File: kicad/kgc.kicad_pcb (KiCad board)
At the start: 2 copper layers, 200 x 100 mm, 36 parts, among them IC1 Pico, IC2 MAX7219, IC3 MAX7219

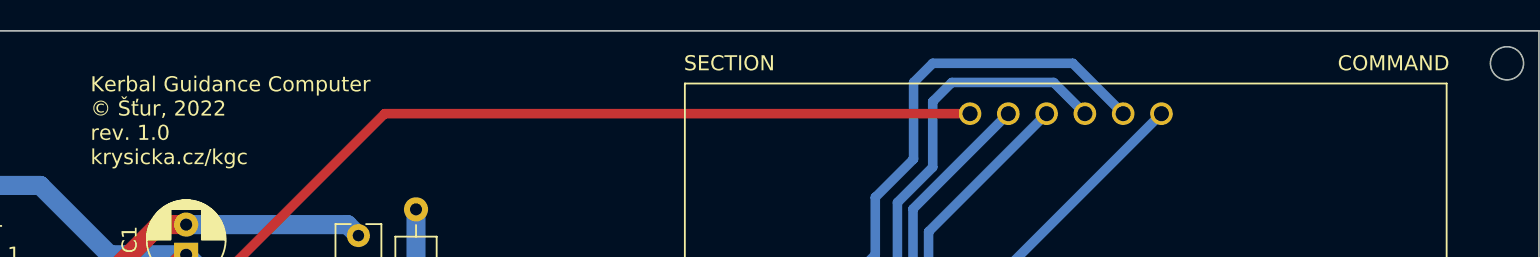
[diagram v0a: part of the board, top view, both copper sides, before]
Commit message: New program switching system, support for LED indicators and buzzer, clear_display now clears individual displays, electrical schematic improvements
kgc.c:
  - New macros for LEDs and buzzer GPIO pins.
  - New function led_init for initializing LEDs and buzzer GPIOs.
  - Section and command system was replaced by verb and nouns (yes, I robed it from AGC). Verbs are commands, nouns are relatively independent parameters for verbs (mostly kind of displayed data) . Verbs are executed by core 0 in main, nouns by core1 in core1_entry.
  - Verbs list:
    - 00 for no operation
    - 01 for display data only
    - 99 for device test
  - Nouns list:
    - 00 for no operation
    - 01 for stopwatch
    - 02 for countdown (doesn't work)

keypad.(h/c):
  - Deleted program and prev_program variables.
  - Renamed section and command variables to verb and noun.

max7219.(h/c):
  - Function clear_display now clears individual display, not whole chip.

kicad:
  - Schematic cleanup.
  - PDF version of schematic included.
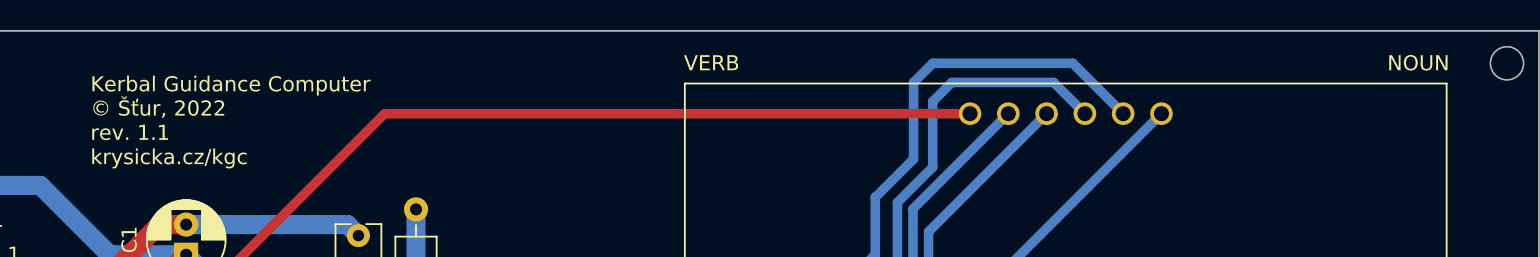
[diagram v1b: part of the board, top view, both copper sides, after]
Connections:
- net /RXD renamed RXD
- net /TXD renamed TXD
- net Net-(BZ1-Pad1) renamed BUZZ
- net Net-(BZ1-Pad2) renamed GND2
- net Net-(C1-Pad2) renamed GND3
- net Net-(DISP1-Pad1) renamed IC2_SEG_E
- net Net-(DISP1-Pad10) renamed IC2_SEG_F
- net Net-(DISP1-Pad11) renamed IC2_SEG_A
- net Net-(DISP1-Pad12) renamed IC2_DIG_0
- net Net-(DISP1-Pad2) renamed IC2_SEG_D
- net Net-(DISP1-Pad3) renamed IC2_SEG_DP
- net Net-(DISP1-Pad4) renamed IC2_SEG_C
- net Net-(DISP1-Pad5) renamed IC2_SEG_G
- net Net-(DISP1-Pad6) renamed IC2_DIG_3
- net Net-(DISP1-Pad7) renamed IC2_SEG_B
- net Net-(DISP1-Pad8) renamed IC2_DIG_2
- net Net-(DISP1-Pad9) renamed IC2_DIG_1
- net Net-(DISP2-Pad12) renamed IC2_DIG_4
- net Net-(DISP2-Pad6) renamed IC2_DIG_7
- net Net-(DISP2-Pad8) renamed IC2_DIG_6
- net Net-(DISP2-Pad9) renamed IC2_DIG_5
- net Net-(DISP3-Pad1) renamed IC3_SEG_E
- net Net-(DISP3-Pad10) renamed IC3_SEG_F
- net Net-(DISP3-Pad11) renamed IC3_SEG_A
- net Net-(DISP3-Pad12) renamed IC3_DIG_0
- net Net-(DISP3-Pad2) renamed IC3_SEG_D
- net Net-(DISP3-Pad3) renamed IC3_SEG_DP
- net Net-(DISP3-Pad4) renamed IC3_SEG_C
- net Net-(DISP3-Pad5) renamed IC3_SEG_G
- net Net-(DISP3-Pad6) renamed IC3_DIG_3
- net Net-(DISP3-Pad7) renamed IC3_SEG_B
- net Net-(DISP3-Pad8) renamed IC3_DIG_2
- net Net-(DISP3-Pad9) renamed IC3_DIG_1
- net Net-(DISP4-Pad12) renamed IC3_DIG_4
- net Net-(DISP4-Pad6) renamed IC3_DIG_7
- net Net-(DISP4-Pad8) renamed IC3_DIG_6
- net Net-(DISP4-Pad9) renamed IC3_DIG_5
- net Net-(IC1-Pad10) renamed LED_ELC
- net Net-(IC1-Pad11) renamed LED_LFO
- net Net-(IC1-Pad12) renamed LED_MOP
- net Net-(IC1-Pad14) renamed LED_OTR
- net Net-(IC1-Pad15) renamed LED_RCS
- net Net-(IC1-Pad16) renamed LED_BRK
- net Net-(IC1-Pad20) renamed KBD_R4
- net Net-(IC1-Pad21) renamed KBD_R3
- net Net-(IC1-Pad22) renamed LOAD_1
- net Net-(IC1-Pad24) renamed CLK
- net Net-(IC1-Pad25) renamed DIN
- net Net-(IC1-Pad26) renamed KBD_R2
- net Net-(IC1-Pad27) renamed KBD_R1
- net Net-(IC1-Pad29) renamed KBD_C4
- net Net-(IC1-Pad3) renamed GND1
- net Net-(IC1-Pad31) renamed KBD_C3
- net Net-(IC1-Pad32) renamed KBD_C2
- net Net-(IC1-Pad34) renamed KBD_C1
- net Net-(IC1-Pad4) renamed LED_CON
- net Net-(IC1-Pad5) renamed LED_FLD
- net Net-(IC1-Pad6) renamed LED_GEA
- net Net-(IC1-Pad7) renamed LOAD_2
- net Net-(IC1-Pad9) renamed LED_SAS
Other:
- board text added: "Kerbal Guidance Computer © Šťur, 2022 rev. 1.1 krysicka.cz/kgc"
- board text added: "NOUN"
- board text added: "VERB"
- board text removed: "COMMAND"
- board text removed: "Kerbal Guidance Computer © Šťur, 2022 rev. 1.0 krysicka.cz/kgc"
- board text removed: "SECTION"

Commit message: Added KiCad project files
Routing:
- net IC2_DIG_4: track 52.5 -> 53.6 mm

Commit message: New hardware revision
- Created new PCB
- KiCad project updated
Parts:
- removed IC1: Pico, mistniBordel:RPi_Pico_TH
- removed IC2, IC3: MAX7219, Package_DIP:DIP-24_W7.62mm
- removed KBD1: ak1604, Connector_PinHeader_2.54mm:PinHeader_1x08_P2.54mm_Vertical
- removed UART1: UART, Connector_PinHeader_2.54mm:PinHeader_1x04_P2.54mm_Horizontal
- added C10: 100n, Capacitor_SMD:C_0603_1608Metric_Pad1.08x0.95mm_HandSolder, B.Cu at (198.1, 86.7)
- added C11: 100n, Capacitor_SMD:C_0603_1608Metric_Pad1.08x0.95mm_HandSolder, B.Cu at (191.2, 99.9)
- added C12: 100n, Capacitor_SMD:C_0603_1608Metric_Pad1.08x0.95mm_HandSolder, B.Cu at (197.5, 91.4)
- added C13: 100n, Capacitor_SMD:C_0603_1608Metric_Pad1.08x0.95mm_HandSolder, B.Cu at (179.5, 93.4)
- added C14: 100n, Capacitor_SMD:C_0603_1608Metric_Pad1.08x0.95mm_HandSolder, B.Cu at (188.4, 98.5)
- added C15: 4.7u, Capacitor_SMD:C_0603_1608Metric_Pad1.08x0.95mm_HandSolder, B.Cu at (182.3, 81.1)
- added C16: 4.7u, Capacitor_SMD:C_0603_1608Metric_Pad1.08x0.95mm_HandSolder, B.Cu at (175.5, 81.1)
- added C17: 4.7u, Capacitor_SMD:C_0603_1608Metric_Pad1.08x0.95mm_HandSolder, B.Cu at (179.5, 87.9)
- added C18: 15p, Capacitor_SMD:C_0603_1608Metric_Pad1.08x0.95mm_HandSolder, B.Cu at (192.0, 105.9)
- added C19: 15p, Capacitor_SMD:C_0603_1608Metric_Pad1.08x0.95mm_HandSolder, B.Cu at (185.6, 105.9)
- added C20: 100n, Capacitor_SMD:C_0603_1608Metric_Pad1.08x0.95mm_HandSolder, B.Cu at (197.2, 73.9)
- added C21: 100 nF, Capacitor_SMD:C_0603_1608Metric_Pad1.08x0.95mm_HandSolder, B.Cu at (160.2, 45.4)
- added C22: 4.7 uF, Capacitor_SMD:CP_Elec_5x4.5, B.Cu at (158.2, 51.3)
- added C23: 100 nF, Capacitor_SMD:C_0603_1608Metric_Pad1.08x0.95mm_HandSolder, B.Cu at (162.3, 44.4)
- added C24: 10 uF, Capacitor_SMD:CP_Elec_5x4.5, B.Cu at (276.1, 52.5)
- added C25: 0.1 uF, Capacitor_SMD:C_0603_1608Metric_Pad1.08x0.95mm_HandSolder, B.Cu at (268.2, 63.4)
- added C26: 10 uF, Capacitor_SMD:CP_Elec_5x4.5, B.Cu at (221.9, 108.9)
- added C27: 0.1 uF, Capacitor_SMD:C_0603_1608Metric_Pad1.08x0.95mm_HandSolder, B.Cu at (214.1, 119.9)
- added C28: 10 uF, Capacitor_SMD:CP_Elec_5x4.5, B.Cu at (221.9, 70.6)
- added C29: 0.1 uF, Capacitor_SMD:C_0603_1608Metric_Pad1.08x0.95mm_HandSolder, B.Cu at (214.1, 81.2)
- added C5: 100n, Capacitor_SMD:C_0603_1608Metric_Pad1.08x0.95mm_HandSolder, B.Cu at (185.6, 99.6)
- added C6: 100n, Capacitor_SMD:C_0603_1608Metric_Pad1.08x0.95mm_HandSolder, B.Cu at (179.5, 84.0)
- added C7: 100n, Capacitor_SMD:C_0603_1608Metric_Pad1.08x0.95mm_HandSolder, B.Cu at (179.5, 86.1)
- added C8: 100n, Capacitor_SMD:C_0603_1608Metric_Pad1.08x0.95mm_HandSolder, B.Cu at (179.5, 89.8)
- added C9: 100n, Capacitor_SMD:C_0603_1608Metric_Pad1.08x0.95mm_HandSolder, B.Cu at (191.4, 81.1)
- added D11: 1N5819, Diode_THT:D_DO-41_SOD81_P7.62mm_Horizontal, B.Cu at (313.2, 191.3)
- added D12: 1N5819, Diode_THT:D_DO-41_SOD81_P7.62mm_Horizontal, B.Cu at (188.2, 178.8)
- added D13: 1N5819, Diode_THT:D_DO-41_SOD81_P7.62mm_Horizontal, B.Cu at (213.3, 178.8)
- added D14: 1N5819, Diode_THT:D_DO-41_SOD81_P7.62mm_Horizontal, B.Cu at (238.3, 178.8)
- added D15: 1N5819, Diode_THT:D_DO-41_SOD81_P7.62mm_Horizontal, B.Cu at (263.3, 178.8)
- added D16: 1N5819, Diode_THT:D_DO-41_SOD81_P7.62mm_Horizontal, B.Cu at (288.3, 178.8)
- added D17: 1N5819, Diode_THT:D_DO-41_SOD81_P7.62mm_Horizontal, B.Cu at (188.2, 203.7)
- added D18: 1N5819, Diode_THT:D_DO-41_SOD81_P7.62mm_Horizontal, B.Cu at (213.2, 203.8)
- added D19: 1N5819, Diode_THT:D_DO-41_SOD81_P7.62mm_Horizontal, B.Cu at (238.3, 203.7)
- added D20: 1N5819, Diode_THT:D_DO-41_SOD81_P7.62mm_Horizontal, B.Cu at (263.4, 203.7)
- added D21: 1N5819, Diode_THT:D_DO-41_SOD81_P7.62mm_Horizontal, B.Cu at (288.3, 203.7)
- added D22: CON, LED_SMD:LED_0805_2012Metric_Pad1.15x1.40mm_HandSolder, F.Cu at (164.6, 50.6)
- added D23: FLD, LED_SMD:LED_0805_2012Metric_Pad1.15x1.40mm_HandSolder, F.Cu at (203.1, 50.6)
- added D24: ELC, LED_SMD:LED_0805_2012Metric_Pad1.15x1.40mm_HandSolder, F.Cu at (164.6, 70.5)
- added D25: MOP, LED_SMD:LED_0805_2012Metric_Pad1.15x1.40mm_HandSolder, F.Cu at (203.1, 70.5)
- added D26: LFO, LED_SMD:LED_0805_2012Metric_Pad1.15x1.40mm_HandSolder, F.Cu at (164.6, 90.3)
- added D27: OTR, LED_SMD:LED_0805_2012Metric_Pad1.15x1.40mm_HandSolder, F.Cu at (203.1, 90.3)
- added D28: SAS, LED_SMD:LED_0805_2012Metric_Pad1.15x1.40mm_HandSolder, F.Cu at (164.6, 110.2)
- added D29: RCS, LED_SMD:LED_0805_2012Metric_Pad1.15x1.40mm_HandSolder, F.Cu at (203.1, 110.2)
- added D30: GEA, LED_SMD:LED_0805_2012Metric_Pad1.15x1.40mm_HandSolder, F.Cu at (164.6, 130.0)
- added D31: BRK, LED_SMD:LED_0805_2012Metric_Pad1.15x1.40mm_HandSolder, F.Cu at (203.1, 130.0)
- added DISP10: OPD-D5631YG-BW, Display_7Segment:DA56-11CGKWA, F.Cu at (240.3, 138.1)
- added DISP11: OPD-D5631YG-BW, Display_7Segment:DA56-11CGKWA, F.Cu at (266.1, 138.1)
- added DISP12: OPD-D5631YG-BW, Display_7Segment:DA56-11CGKWA, F.Cu at (291.9, 138.1)
- added DISP5: OPD-D5631YG-BW, Display_7Segment:DA56-11CGKWA, F.Cu at (266.1, 98.1)
- added DISP6: OPD-D5631YG-BW, Display_7Segment:DA56-11CGKWA, F.Cu at (291.9, 98.1)
- added DISP7: OPD-D5631YG-BW, Display_7Segment:DA56-11CGKWA, F.Cu at (240.3, 118.1)
- added DISP8: OPD-D5631YG-BW, Display_7Segment:DA56-11CGKWA, F.Cu at (266.1, 118.1)
- added DISP9: OPD-D5631YG-BW, Display_7Segment:DA56-11CGKWA, F.Cu at (291.9, 118.1)
- added H1: MountingHole, MountingHole:MountingHole_3.2mm_M3, F.Cu at (135.0, 35.0)
- added H2: MountingHole, MountingHole:MountingHole_3.2mm_M3, F.Cu at (325.0, 35.0)
- added H3: MountingHole, MountingHole:MountingHole_3.2mm_M3, F.Cu at (325.0, 235.0)
- added H4: MountingHole, MountingHole:MountingHole_3.2mm_M3, F.Cu at (135.0, 235.0)
- added J1: Conn_01x04_Pin, Connector_PinHeader_2.54mm:PinHeader_1x04_P2.54mm_Horizontal, B.Cu at (159.3, 89.0)
- added J2: SM03B-SRSS-TB, Connector_JST:JST_SH_SM03B-SRSS-TB_1x03-1MP_P1.00mm_Horizontal, B.Cu at (157.2, 103.2)
- added J4: USB_C_Receptacle_USB2.0_16P, Connector_USB:USB_C_Receptacle_GCT_USB4085, B.Cu at (175.0, 36.1)
- added J5: USB_C_Receptacle_USB2.0_16P, Connector_USB:USB_C_Receptacle_GCT_USB4085, B.Cu at (150.0, 36.1)
- added L1: 3.3u, RP2350_80QFN:L_pol_2016, B.Cu at (179.3, 81.2)
- added R13: 5k, Resistor_SMD:R_0603_1608Metric_Pad0.98x0.95mm_HandSolder, F.Cu at (153.0, 32.1)
- added R14: 27R, Resistor_SMD:R_0603_1608Metric_Pad0.98x0.95mm_HandSolder, B.Cu at (157.9, 40.4)
- added R15: 27R, Resistor_SMD:R_0603_1608Metric_Pad0.98x0.95mm_HandSolder, B.Cu at (152.4, 40.4)
- added R16: 270R, Resistor_SMD:R_0603_1608Metric_Pad0.98x0.95mm_HandSolder, B.Cu at (139.8, 43.4)
- added R17: 270R, Resistor_SMD:R_0603_1608Metric_Pad0.98x0.95mm_HandSolder, B.Cu at (139.8, 45.9)
- added R18: 1k, Resistor_SMD:R_0603_1608Metric_Pad0.98x0.95mm_HandSolder, B.Cu at (182.8, 143.7)
- added R19: 1k, Resistor_SMD:R_0603_1608Metric_Pad0.98x0.95mm_HandSolder, B.Cu at (185.4, 143.7)
- added R20: 1k, Resistor_SMD:R_0603_1608Metric_Pad0.98x0.95mm_HandSolder, B.Cu at (187.9, 143.7)
- added R21: 1k, Resistor_SMD:R_0603_1608Metric_Pad0.98x0.95mm_HandSolder, B.Cu at (190.5, 143.7)
- added R22: 1k, Resistor_SMD:R_0603_1608Metric_Pad0.98x0.95mm_HandSolder, B.Cu at (193.0, 143.7)
- added R23: 1k, Resistor_SMD:R_0603_1608Metric_Pad0.98x0.95mm_HandSolder, B.Cu at (195.5, 143.7)
- added R24: 1k, Resistor_SMD:R_0603_1608Metric_Pad0.98x0.95mm_HandSolder, B.Cu at (198.1, 143.7)
- added R25: 10k, Resistor_SMD:R_0603_1608Metric_Pad0.98x0.95mm_HandSolder, B.Cu at (268.2, 65.1)
- added R26: 10k, Resistor_SMD:R_0603_1608Metric_Pad0.98x0.95mm_HandSolder, B.Cu at (214.1, 121.5)
- added R27: 10k, Resistor_SMD:R_0603_1608Metric_Pad0.98x0.95mm_HandSolder, B.Cu at (214.1, 82.8)
- added R28: 100R, Resistor_SMD:R_0603_1608Metric_Pad0.98x0.95mm_HandSolder, F.Cu at (171.6, 50.6)
- added R29: 100R, Resistor_SMD:R_0603_1608Metric_Pad0.98x0.95mm_HandSolder, F.Cu at (210.1, 50.6)
- added R30: 100R, Resistor_SMD:R_0603_1608Metric_Pad0.98x0.95mm_HandSolder, F.Cu at (171.6, 70.5)
- added R31: 100R, Resistor_SMD:R_0603_1608Metric_Pad0.98x0.95mm_HandSolder, F.Cu at (210.1, 70.5)
- added R32: 100R, Resistor_SMD:R_0603_1608Metric_Pad0.98x0.95mm_HandSolder, F.Cu at (171.6, 90.3)
- added R33: 100R, Resistor_SMD:R_0603_1608Metric_Pad0.98x0.95mm_HandSolder, F.Cu at (210.1, 90.3)
- added R34: 100R, Resistor_SMD:R_0603_1608Metric_Pad0.98x0.95mm_HandSolder, F.Cu at (171.6, 110.2)
- added R35: 100R, Resistor_SMD:R_0603_1608Metric_Pad0.98x0.95mm_HandSolder, F.Cu at (210.1, 110.2)
- added R36: 100R, Resistor_SMD:R_0603_1608Metric_Pad0.98x0.95mm_HandSolder, F.Cu at (171.6, 130.0)
- added R37: 100R, Resistor_SMD:R_0603_1608Metric_Pad0.98x0.95mm_HandSolder, F.Cu at (210.1, 130.0)
- added SW1: TS6606, Button_Switch_THT:SW_Tactile_SKHH_Angled, B.Cu at (283.4, 32.8)
- added SW10: ., other_things:SW_Cherry_MX_1.00u_PCB, F.Cu at (182.5, 184.9)
- added SW11: 4, other_things:SW_Cherry_MX_1.00u_PCB, F.Cu at (207.5, 184.9)
- added SW12: 5, other_things:SW_Cherry_MX_1.00u_PCB, F.Cu at (232.5, 184.9)
- added SW13: 6, other_things:SW_Cherry_MX_1.00u_PCB, F.Cu at (257.5, 184.9)
- added SW14: PRO, other_things:SW_Cherry_MX_1.00u_PCB, F.Cu at (282.5, 184.9)
- added SW15: NOUN, other_things:SW_Cherry_MX_1.00u_PCB, F.Cu at (157.5, 197.4)
- added SW16: ALRM, other_things:SW_Cherry_MX_1.00u_PCB, F.Cu at (307.5, 197.4)
- added SW17: 0, other_things:SW_Cherry_MX_1.00u_PCB, F.Cu at (182.5, 209.9)
- added SW18: 1, other_things:SW_Cherry_MX_1.00u_PCB, F.Cu at (207.5, 209.9)
- added SW19: 2, other_things:SW_Cherry_MX_1.00u_PCB, F.Cu at (232.5, 209.9)
- added SW2: TS6606, Button_Switch_THT:SW_Tactile_SKHH_Angled, B.Cu at (308.4, 32.8)
- added SW20: 3, other_things:SW_Cherry_MX_1.00u_PCB, F.Cu at (257.5, 209.9)
- added SW21: RSET, other_things:SW_Cherry_MX_1.00u_PCB, F.Cu at (282.5, 209.9)
- added SW3: -, other_things:SW_Cherry_MX_1.00u_PCB, F.Cu at (182.5, 159.9)
- added SW4: 7, other_things:SW_Cherry_MX_1.00u_PCB, F.Cu at (207.5, 159.9)
- added SW5: 8, other_things:SW_Cherry_MX_1.00u_PCB, F.Cu at (232.5, 159.9)
- added SW6: 9, other_things:SW_Cherry_MX_1.00u_PCB, F.Cu at (257.5, 159.9)
- added SW7: CLR, other_things:SW_Cherry_MX_1.00u_PCB, F.Cu at (282.5, 159.9)
- added SW8: VERB, other_things:SW_Cherry_MX_1.00u_PCB, F.Cu at (157.5, 172.4)
- added SW9: ENTR, other_things:SW_Cherry_MX_1.00u_PCB, F.Cu at (307.5, 172.4)
- added TP1: TestPoint, TestPoint:TestPoint_Plated_Hole_D2.0mm, F.Cu at (279.5, 75.7)
- added TP2: TestPoint, TestPoint:TestPoint_Plated_Hole_D2.0mm, F.Cu at (149.2, 48.0)
- added TP3: TestPoint, TestPoint:TestPoint_Plated_Hole_D2.0mm, F.Cu at (214.1, 135.2)
- added TP4: TestPoint, TestPoint:TestPoint_Plated_Hole_D2.0mm, F.Cu at (160.7, 59.5)
- added TP5: TestPoint, TestPoint:TestPoint_Plated_Hole_D2.0mm, F.Cu at (225.6, 99.0)
- added TP6: TestPoint, TestPoint:TestPoint_Plated_Hole_D2.0mm, F.Cu at (181.2, 60.7)
- added TP7: TestPoint, TestPoint:TestPoint_Plated_Hole_D2.0mm, F.Cu at (208.4, 99.0)
- added TP8: TestPoint, TestPoint:TestPoint_Plated_Hole_D2.0mm, F.Cu at (148.5, 54.8)
- added TP9: TestPoint, TestPoint:TestPoint_Plated_Hole_D2.0mm, F.Cu at (217.0, 99.0)
- added U1: NCP1117-3.3_SOT223, Package_TO_SOT_SMD:SOT-223-3_TabPin2, B.Cu at (166.3, 63.2)
- added U2: RP2350_80QFN, RP2350_80QFN:RP2350-QFN-80-1EP_10x10_P0.4mm_EP3.4x3.4mm_ThermalVias, B.Cu at (188.5, 89.6)
- added U3: W25Q128JVS, Package_SO:SOIC-8_5.3x5.3mm_P1.27mm, B.Cu at (201.9, 77.9)
- added U4: FT230XS, Package_SO:SSOP-16_3.9x4.9mm_P0.635mm, B.Cu at (155.1, 44.9)
- added U5: MAX7221xWG, Package_SO:SOIC-24W_7.5x15.4mm_P1.27mm, B.Cu at (276.3, 64.0)
- added U6: MAX7221xWG, Package_SO:SOIC-24W_7.5x15.4mm_P1.27mm, B.Cu at (222.1, 120.5)
- added U7: MAX7221xWG, Package_SO:SOIC-24W_7.5x15.4mm_P1.27mm, B.Cu at (222.2, 81.8)
- added Y1: ABM8-272-T3, Crystal:Crystal_SMD_3225-4Pin_3.2x2.5mm, B.Cu at (188.8, 106.1)
- BZ1: footprint Buzzer_Beeper:Buzzer_12x9.5RM7.6 -> other_things:Buzzer_XDCR_CPT-1203-03-SMT-TR; moved to B.Cu
- C1: value 10 uF -> 10u; footprint Capacitor_THT:CP_Radial_D5.0mm_P2.00mm -> Capacitor_SMD:C_0603_1608Metric_Pad1.08x0.95mm_HandSolder; moved to B.Cu
- C2: value 0.1 uF -> 10u; footprint mistniBordel:C31x -> Capacitor_SMD:C_0603_1608Metric_Pad1.08x0.95mm_HandSolder; moved to B.Cu
- C3: value 10 uF -> 100n; footprint Capacitor_THT:CP_Radial_D5.0mm_P2.00mm -> Capacitor_SMD:C_0603_1608Metric_Pad1.08x0.95mm_HandSolder; moved to B.Cu
- C4: value 0.1 uF -> 4.7u; footprint mistniBordel:C31x -> Capacitor_SMD:C_0603_1608Metric_Pad1.08x0.95mm_HandSolder; moved to B.Cu
- D1: value CON -> RXLED; footprint LED_THT:LED_D5.0mm -> LED_SMD:LED_0603_1608Metric; moved to B.Cu
- D10: value BRK -> 1N5819; footprint LED_THT:LED_D5.0mm -> Diode_THT:D_DO-41_SOD81_P7.62mm_Horizontal; moved to B.Cu
- D2: value FLD -> TXLED; footprint LED_THT:LED_D5.0mm -> LED_SMD:LED_0603_1608Metric; moved to B.Cu
- D3: value ELC -> 1N5819; footprint LED_THT:LED_D5.0mm -> Diode_THT:D_DO-41_SOD81_P7.62mm_Horizontal; moved to B.Cu
- D4: value MOP -> 1N5819; footprint LED_THT:LED_D5.0mm -> Diode_THT:D_DO-41_SOD81_P7.62mm_Horizontal; moved to B.Cu
- D5: value LFO -> 1N5819; footprint LED_THT:LED_D5.0mm -> Diode_THT:D_DO-41_SOD81_P7.62mm_Horizontal; moved to B.Cu
- D6: value OTR -> 1N5819; footprint LED_THT:LED_D5.0mm -> Diode_THT:D_DO-41_SOD81_P7.62mm_Horizontal; moved to B.Cu
- D7: value SAS -> 1N5819; footprint LED_THT:LED_D5.0mm -> Diode_THT:D_DO-41_SOD81_P7.62mm_Horizontal; moved to B.Cu
- D8: value RCS -> 1N5819; footprint LED_THT:LED_D5.0mm -> Diode_THT:D_DO-41_SOD81_P7.62mm_Horizontal; moved to B.Cu
- D9: value GEA -> 1N5819; footprint LED_THT:LED_D5.0mm -> Diode_THT:D_DO-41_SOD81_P7.62mm_Horizontal; moved to B.Cu
- DISP1, DISP2, DISP3, DISP4: value CC56-12GWA -> OPD-D5631YG-BW; footprint Display_7Segment:CC56-12GWA -> Display_7Segment:DA56-11CGKWA
- R1: value 100R -> 33; footprint Resistor_THT:R_Axial_DIN0207_L6.3mm_D2.5mm_P10.16mm_Horizontal -> Resistor_SMD:R_0603_1608Metric_Pad0.98x0.95mm_HandSolder; moved to B.Cu
- R10: value 100R -> 5k; footprint Resistor_THT:R_Axial_DIN0207_L6.3mm_D2.5mm_P10.16mm_Horizontal -> Resistor_SMD:R_0603_1608Metric_Pad0.98x0.95mm_HandSolder
- R11: value 10k -> 5k; footprint Resistor_THT:R_Axial_DIN0207_L6.3mm_D2.5mm_P10.16mm_Horizontal -> Resistor_SMD:R_0603_1608Metric_Pad0.98x0.95mm_HandSolder
- R12: value 10k -> 5k; footprint Resistor_THT:R_Axial_DIN0207_L6.3mm_D2.5mm_P10.16mm_Horizontal -> Resistor_SMD:R_0603_1608Metric_Pad0.98x0.95mm_HandSolder; moved to B.Cu
- R2, R3: value 100R -> 27R; footprint Resistor_THT:R_Axial_DIN0207_L6.3mm_D2.5mm_P10.16mm_Horizontal -> Resistor_SMD:R_0603_1608Metric_Pad0.98x0.95mm_HandSolder; moved to B.Cu
- R4, R5, R6: value 100R -> 1k; footprint Resistor_THT:R_Axial_DIN0207_L6.3mm_D2.5mm_P10.16mm_Horizontal -> Resistor_SMD:R_0603_1608Metric_Pad0.98x0.95mm_HandSolder; moved to B.Cu
- R7, R8: value 100R -> DNF; footprint Resistor_THT:R_Axial_DIN0207_L6.3mm_D2.5mm_P10.16mm_Horizontal -> Resistor_SMD:R_0603_1608Metric_Pad0.98x0.95mm_HandSolder; moved to B.Cu
- R9: value 100R -> 0R; footprint Resistor_THT:R_Axial_DIN0207_L6.3mm_D2.5mm_P10.16mm_Horizontal -> Resistor_SMD:R_0603_1608Metric_Pad0.98x0.95mm_HandSolder; moved to B.Cu
- moved D4 248.0 mm to (313.2, 166.1), turned to 180 degrees
- moved R5 240.1 mm to (300.4, 32.9)
- moved D9 235.2 mm to (288.3, 153.8), turned to 180 degrees
- moved D7 187.5 mm to (238.3, 153.8), turned to 180 degrees
- moved D8 187.1 mm to (263.3, 153.8), turned to 180 degrees
- moved R4 186.3 mm to (275.4, 32.9)
- moved R9 144.1 mm to (201.9, 81.8), turned to 0 degrees
- moved D5 143.8 mm to (188.3, 153.8), turned to 180 degrees
- moved D6 143.4 mm to (213.3, 153.8), turned to 180 degrees
- moved R7 141.6 mm to (203.2, 72.1), turned to 0 degrees
- moved D3 136.6 mm to (163.3, 166.2), turned to 180 degrees
- moved R10 129.6 mm to (174.3, 38.6)
- moved R8 119.1 mm to (204.9, 73.9)
- moved R3 115.1 mm to (186.1, 81.1), turned to 90 degrees
- moved R1 109.4 mm to (180.0, 76.7), turned to 0 degrees
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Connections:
- BZ1 pad 1: BUZZ -> /BUZZ
- BZ1 pad 2: GND2 -> GND
- C1 pad 1: +5V -> VBUS
- C1 pad 2: GND3 -> GND
- C2 pad 1: +5V -> +3V3
- C2 pad 2: GND3 -> GND
- C3 pad 1: +5V -> +1V1
- C3 pad 2: GND3 -> GND
- C4 pad 1: +5V -> +1V1
- C4 pad 2: GND3 -> GND
- D1 pad 1: GND2 -> Net-(D1-K)
- D1 pad 2: Net-(D1-Pad2) -> Net-(D1-A)
- D10 pad 1: GND2 -> /KBD_ROW_2
- D10 pad 2: Net-(D10-Pad2) -> Net-(D10-A)
- D2 pad 1: GND2 -> Net-(D2-K)
- D2 pad 2: Net-(D2-Pad2) -> Net-(D2-A)
- D3 pad 1: GND2 -> /KBD_ROW_1
- D3 pad 2: Net-(D3-Pad2) -> Net-(D3-A)
- D4 pad 1: GND2 -> /KBD_ROW_1
- D4 pad 2: Net-(D4-Pad2) -> Net-(D4-A)
- D5 pad 1: GND2 -> /KBD_ROW_1
- D5 pad 2: Net-(D5-Pad2) -> Net-(D5-A)
- D6 pad 1: GND2 -> /KBD_ROW_1
- D6 pad 2: Net-(D6-Pad2) -> Net-(D6-A)
- D7 pad 1: GND2 -> /KBD_ROW_1
- D7 pad 2: Net-(D7-Pad2) -> Net-(D7-A)
- D8 pad 1: GND2 -> /KBD_ROW_1
- D8 pad 2: Net-(D8-Pad2) -> Net-(D8-A)
- D9 pad 1: GND2 -> /KBD_ROW_1
- D9 pad 2: Net-(D9-Pad2) -> Net-(D9-A)
- DISP1 pad 1: IC2_SEG_E -> /Displays and LEDs/MAX3_SEG_E
- DISP1 pad 10: IC2_SEG_F -> /Displays and LEDs/MAX3_SEG_B
- DISP1 pad 11: IC2_SEG_A -> /Displays and LEDs/MAX3_SEG_A
- DISP1 pad 12: IC2_DIG_0 -> /Displays and LEDs/MAX3_SEG_F
- DISP1 pad 2: IC2_SEG_D -> /Displays and LEDs/MAX3_SEG_D
- DISP1 pad 3: IC2_SEG_DP -> /Displays and LEDs/MAX3_SEG_C
- DISP1 pad 4: IC2_SEG_C -> /Displays and LEDs/MAX3_SEG_DP
- DISP1 pad 5: IC2_SEG_G -> /Displays and LEDs/MAX3_SEG_E
- DISP1 pad 6: IC2_DIG_3 -> /Displays and LEDs/MAX3_SEG_D
- DISP1 pad 7: IC2_SEG_B -> /Displays and LEDs/MAX3_SEG_G
- DISP1 pad 8: IC2_DIG_2 -> /Displays and LEDs/MAX3_SEG_C
- DISP1 pad 9: IC2_DIG_1 -> /Displays and LEDs/MAX3_SEG_DP
- DISP2 pad 1: IC2_SEG_E -> /Displays and LEDs/MAX1_SEG_E
- DISP2 pad 10: IC2_SEG_F -> /Displays and LEDs/MAX1_SEG_B
- DISP2 pad 11: IC2_SEG_A -> /Displays and LEDs/MAX1_SEG_A
- DISP2 pad 12: IC2_DIG_4 -> /Displays and LEDs/MAX1_SEG_F
- DISP2 pad 2: IC2_SEG_D -> /Displays and LEDs/MAX1_SEG_D
- DISP2 pad 3: IC2_SEG_DP -> /Displays and LEDs/MAX1_SEG_C
- DISP2 pad 4: IC2_SEG_C -> /Displays and LEDs/MAX1_SEG_DP
- DISP2 pad 5: IC2_SEG_G -> /Displays and LEDs/MAX1_SEG_E
- DISP2 pad 6: IC2_DIG_7 -> /Displays and LEDs/MAX1_SEG_D
- DISP2 pad 7: IC2_SEG_B -> /Displays and LEDs/MAX1_SEG_G
- DISP2 pad 8: IC2_DIG_6 -> /Displays and LEDs/MAX1_SEG_C
- DISP2 pad 9: IC2_DIG_5 -> /Displays and LEDs/MAX1_SEG_DP
- DISP3 pad 1: IC3_SEG_E -> /Displays and LEDs/MAX1_SEG_E
- DISP3 pad 10: IC3_SEG_F -> /Displays and LEDs/MAX1_SEG_B
- DISP3 pad 11: IC3_SEG_A -> /Displays and LEDs/MAX1_SEG_A
- DISP3 pad 12: IC3_DIG_0 -> /Displays and LEDs/MAX1_SEG_F
- DISP3 pad 2: IC3_SEG_D -> /Displays and LEDs/MAX1_SEG_D
- DISP3 pad 3: IC3_SEG_DP -> /Displays and LEDs/MAX1_SEG_C
- DISP3 pad 4: IC3_SEG_C -> /Displays and LEDs/MAX1_SEG_DP
- DISP3 pad 5: IC3_SEG_G -> /Displays and LEDs/MAX1_SEG_E
- DISP3 pad 6: IC3_DIG_3 -> /Displays and LEDs/MAX1_SEG_D
- DISP3 pad 7: IC3_SEG_B -> /Displays and LEDs/MAX1_SEG_G
- DISP3 pad 8: IC3_DIG_2 -> /Displays and LEDs/MAX1_SEG_C
- DISP3 pad 9: IC3_DIG_1 -> /Displays and LEDs/MAX1_SEG_DP
- DISP4 pad 1: IC3_SEG_E -> /Displays and LEDs/MAX3_SEG_E
- DISP4 pad 10: IC3_SEG_F -> /Displays and LEDs/MAX3_SEG_B
- DISP4 pad 11: IC3_SEG_A -> /Displays and LEDs/MAX3_SEG_A
- DISP4 pad 12: IC3_DIG_4 -> /Displays and LEDs/MAX3_SEG_F
- DISP4 pad 2: IC3_SEG_D -> /Displays and LEDs/MAX3_SEG_D
- DISP4 pad 3: IC3_SEG_DP -> /Displays and LEDs/MAX3_SEG_C
- DISP4 pad 4: IC3_SEG_C -> /Displays and LEDs/MAX3_SEG_DP
- DISP4 pad 5: IC3_SEG_G -> /Displays and LEDs/MAX3_SEG_E
- DISP4 pad 6: IC3_DIG_7 -> /Displays and LEDs/MAX3_SEG_D
- DISP4 pad 7: IC3_SEG_B -> /Displays and LEDs/MAX3_SEG_G
- DISP4 pad 8: IC3_DIG_6 -> /Displays and LEDs/MAX3_SEG_C
- DISP4 pad 9: IC3_DIG_5 -> /Displays and LEDs/MAX3_SEG_DP
- R1 pad 1: LED_CON -> +3V3
- R1 pad 2: Net-(D1-Pad2) -> Net-(U2-VREG_AVDD)
- R10 pad 1: LED_BRK -> Net-(J4-CC1)
- R10 pad 2: Net-(D10-Pad2) -> VBUS
- R11 pad 2: +5V -> VBUS
- R12 pad 2: +5V -> VBUS
- R2 pad 1: LED_FLD -> Net-(U2-USB_DP)
- R2 pad 2: Net-(D2-Pad2) -> /USB D+
- R3 pad 1: LED_ELC -> Net-(U2-USB_DM)
- R3 pad 2: Net-(D3-Pad2) -> /USB D-
- R4 pad 1: LED_MOP -> Net-(R4-Pad1)
- R4 pad 2: Net-(D4-Pad2) -> /QSPI_SS
- R5 pad 1: LED_LFO -> Net-(R5-Pad1)
- R5 pad 2: Net-(D5-Pad2) -> Net-(U2-RUN)
- R6 pad 1: LED_OTR -> /XOUT
- R6 pad 2: Net-(D6-Pad2) -> Net-(C19-Pad1)
- R7 pad 1: LED_SAS -> /UART0_TX
- R7 pad 2: Net-(D7-Pad2) -> /FLASH_SS
- R8 pad 1: LED_RCS -> +3V3
- R8 pad 2: Net-(D8-Pad2) -> /FLASH_SS
- R9 pad 1: LED_GEA -> /QSPI_SS
- R9 pad 2: Net-(D9-Pad2) -> /FLASH_SS
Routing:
- net VBUS: track 0.00 -> 333.2 mm, vias 0 -> 10
- net /Displays and LEDs/MAX3_SEG_A: track 0.00 -> 278.7 mm, vias 0 -> 6
- net /Displays and LEDs/MAX3_SEG_C: track 0.00 -> 278.7 mm, vias 0 -> 3
- net /Displays and LEDs/MAX3_SEG_G: track 0.00 -> 270.8 mm, vias 0 -> 3
- net /KBD_ROW_2: track 0.00 -> 268.4 mm, vias 0 -> 2
- net /Displays and LEDs/MAX3_SEG_DP: track 0.00 -> 267.8 mm, vias 0 -> 6
- net Net-(U2-RUN): track 0.00 -> 266.5 mm
- net GND2: track 263.5 -> 0.00 mm
- net /Displays and LEDs/MAX1_SEG_D: track 0.00 -> 260.2 mm, vias 0 -> 2
- net /Displays and LEDs/MAX3_SEG_D: track 0.00 -> 259.5 mm, vias 0 -> 4
- net /KBD_ROW_3: track 0.00 -> 257.7 mm, vias 0 -> 2
- net /Displays and LEDs/MAX3_SEG_B: track 0.00 -> 257.4 mm, vias 0 -> 2
- net /Displays and LEDs/MAX2_SEG_G: track 0.00 -> 255.8 mm, vias 0 -> 2
- net /KBD_ROW_1: track 0.00 -> 242.6 mm, vias 0 -> 1
- net /Displays and LEDs/MAX3_SEG_F: track 0.00 -> 235.9 mm, vias 0 -> 1
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- added copper zone on B.Cu, net +1V1
- added copper zone on B.Cu, net +3V3
- added copper zone on B.Cu, net GND
- added copper zone on F.Cu, net GND
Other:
- board size 200 x 100 mm -> 200 x 210 mm
- board text added: "DSKY for Kerbal Guidance Computer © Šťur, 2025 rev. 2.0 https://github.com/szczurkosmiczny/kgc"
- board text added: "JLCJLCJLCJLC"
- board text added: "M3"
- board text added: "SPI1_MOSI"
- board text added: "SPI1_SCK"
- board text added: "UART1_CTS"
- board text added: "UART1_RTS"
- board text added: "UART1_RX"
- board text added: "UART1_TX"
- board text added: "~{SPI1_SS1}"
- board text added: "~{SPI1_SS2}"
- board text added: "~{SPI1_SS3}"
- board text removed: "+5V"
- board text removed: "1"
- board text removed: "BRK"
- board text removed: "CON"
- board text removed: "ELC"
- board text removed: "FLD"
- board text removed: "GEA"
- board text removed: "GND"
- board text removed: "Kerbal Guidance Computer © Šťur, 2022 rev. 1.1 krysicka.cz/kgc"
- board text removed: "LFO"
- board text removed: "MOP"
- board text removed: "NOUN"
- board text removed: "OTR"
- board text removed: "RCS"
- board text removed: "RX"
- board text removed: "SAS"
- board text removed: "TX"
- board text removed: "VERB"
